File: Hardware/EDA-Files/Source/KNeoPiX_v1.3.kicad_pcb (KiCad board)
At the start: 4 copper layers, 24.5 x 34.6 mm, 35 parts, among them J1 Conn_KNX, J2 Conn_KNX, J3 Screw Terminal - Non Isolated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, J4 Screw Terminal - Isolated IOs, J5 Conn_01x05, J6 Conn_01x05, SW1 Prog BTN, U1 Seeeduino XIAO, U2 LM2937IMP-3.3 / 5.0, U3 ADuM1201AR / ADum1250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

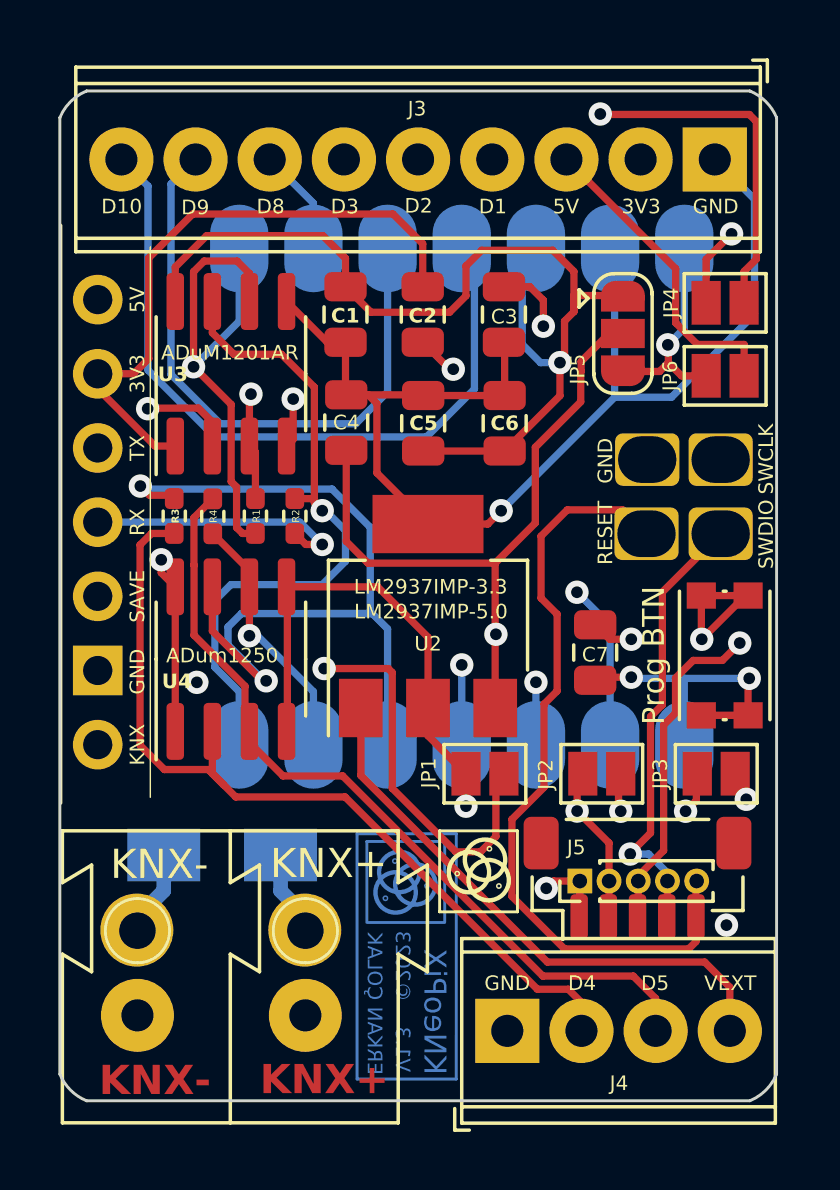
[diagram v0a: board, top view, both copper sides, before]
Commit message: Update - KiCad 8.0x
- Fixed Spelling in sch!
- Ignore Thumbs.db
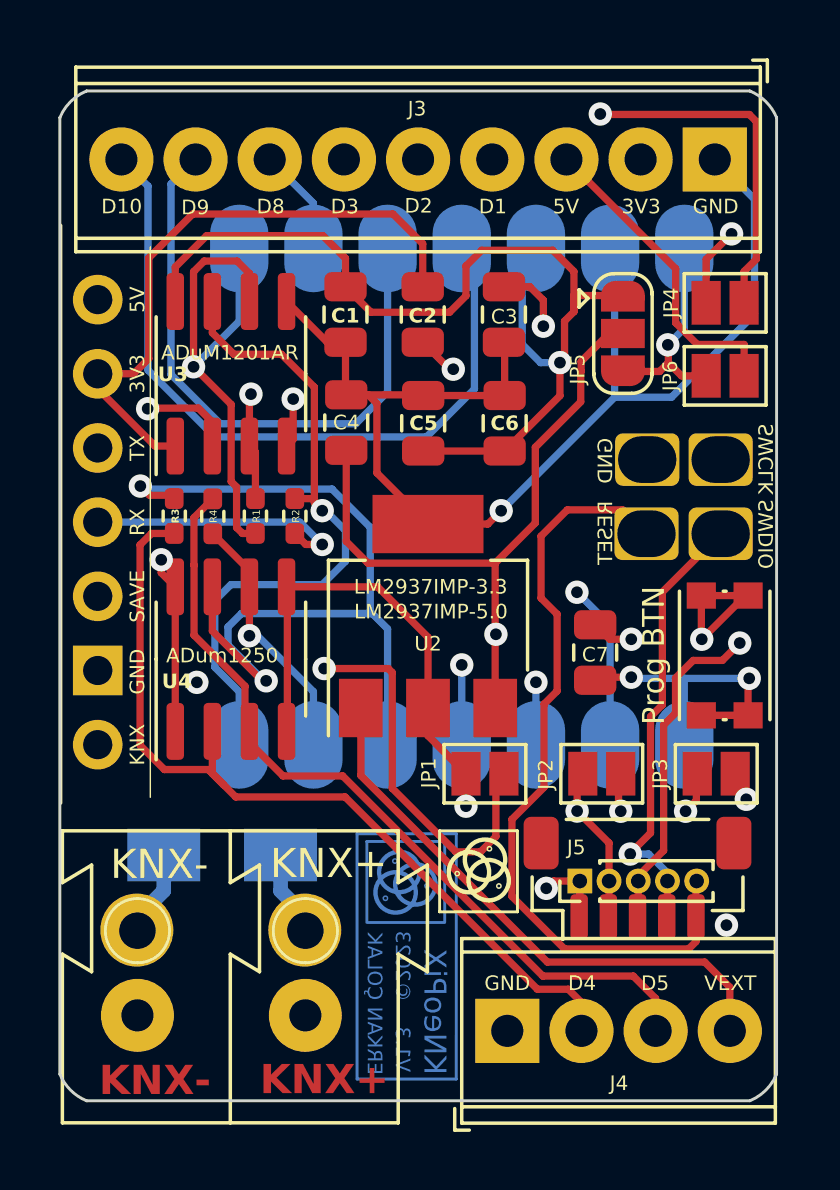
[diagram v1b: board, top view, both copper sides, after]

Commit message: V1.4 - First Prototype Pre Production - In Review
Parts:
- removed the C1 at (58.1, 47.1)
- removed D3: SMAJ40CA-13-F, KNeoPix:D_SMA
- removed J6: Conn_01x05, KNeoPix:PinHeader_1x05_P1.00mm_Vertical
- removed the JP2 at (66.9, 62.8)
- removed JP3: VCC Direct In/Out 3V3/5V, KNeoPix:SolderJumper-2_P1.3mm_Open_Pad1.0x1.5mm
- removed JP6: 5V KNX voltage input, KNeoPix:SolderJumper-2_P1.3mm_Open_Pad1.0x1.5mm
- removed R1: 0Ohm - TXRX Jumper, KNeoPix:R_0402_1005Metric_Pad0.72x0.64mm_HandSolder
- removed R2: 0Ohm - RXTX Jumper, KNeoPix:R_0402_1005Metric_Pad0.72x0.64mm_HandSolder
- removed R3: 0Ohm - D4 Jumper, KNeoPix:R_0402_1005Metric_Pad0.72x0.64mm_HandSolder
- removed R4: 0Ohm - D5 Jumper, KNeoPix:R_0402_1005Metric_Pad0.72x0.64mm_HandSolder
- removed U4: ADum1250, KNeoPix:SOIC-8_3.9x4.9mm_P1.27mm
- added C10: 22uf/16V, Capacitor_SMD:C_0805_2012Metric, F.Cu at (59.7, 47.1)
- added C5: 100nF/16v, Capacitor_SMD:C_01005_0402Metric, F.Cu at (69.0, 57.1)
- added C8: 100nF/50v, Capacitor_SMD:C_0805_2012Metric, F.Cu at (62.0, 63.5)
- added C9: 22uf/16V, Capacitor_SMD:C_0805_2012Metric, F.Cu at (61.9, 47.1)
- added D1: DIODE SCHOTTKY 40V SOD-323HE, lcsc:SOD-323_L1.7-W1.3-LS2.6-RD-1, F.Cu at (70.3, 63.6)
- added D2: DIODE SCHOTTKY 40V SOD-323HE, lcsc:SOD-323_L1.7-W1.3-LS2.6-RD-1, F.Cu at (65.7, 63.6)
- added JP5: SolderJumper_3_Bridged12, Jumper:SolderJumper-3_P1.3mm_Bridged2Bar12_Pad1.0x1.5mm, B.Cu at (64.0, 66.5)
- added L1: CR5040-4R7M, lcsc:IND-SMD_L5.0-W5.0, F.Cu at (66.0, 59.6)
- added U5: AP63205WU-7, lcsc:TSOT-26_L2.9-W1.6-P0.95-LS2.8-BL, F.Cu at (61.2, 52.3)
- C1: renamed from C2; value 100nF -> 100nF/16v; footprint KNeoPix:C_0805_2012Metric -> Capacitor_SMD:C_01005_0402Metric
- C2: renamed from C5; value 100nF -> 100nF/16v; footprint KNeoPix:C_0805_2012Metric -> Capacitor_SMD:C_01005_0402Metric
- C3: value 100 nf 25V -> 100nF/16v; footprint KNeoPix:C_0805_2012Metric -> Capacitor_SMD:C_01005_0402Metric
- C4: value 10µf 16V -> 100nF/16v; footprint KNeoPix:C_0805_2012Metric -> Capacitor_SMD:C_01005_0402Metric
- C6: value 100nF -> 10uf/50V; footprint KNeoPix:C_0805_2012Metric -> Capacitor_SMD:C_0805_2012Metric
- C7: value 100nF 16V - (X5R 0805) -> 10uf/50V; footprint KNeoPix:C_0805_2012Metric -> Capacitor_SMD:C_0805_2012Metric
- J3: value Screw Terminal - Non Isolated IOs -> Screw Terminal - Isolated IOs
- J5: value Conn_01x05 -> ~; footprint KNeoPix:JST_SH_BM05B-SRSS-TB_1x05-1MP_P1.00mm_Vertical -> Connector_JST:JST_SH_BM05B-SRSS-TB_1x05-1MP_P1.00mm_Vertical
- JP1: value GND KNX voltage input -> KNX GND Input; moved to B.Cu
- JP2: renamed from JP5; value Select U2 and Input Voltage -> EXT Input Voltage; moved to B.Cu
- JP4: moved to B.Cu
- SW1: value Prog BTN -> PROG BUTTON; footprint KNeoPix:SW_Push_1P1T_NO_CK_KMR2 -> lcsc:KEY-SMD_4P-L4.2-W3.2-P2.20-LS4.6
- U1: footprint KNeoPix:Seeeduino XIAO-MOUDLE14P-2.54-21X17.8MM-no-15-16-17-18-19-20-pad -> Xiao-ESP32S3-Extendet-Pads:Seeeduino XIAO-MOUDLE14P-2.54-21X17.8MM-no-15-16-17-18-19-20-pad
- U2: value LM2937IMP-3.3 / 5.0 -> TXS0108EPWR; footprint KNeoPix:SOT-223-3_TabPin2 -> lcsc:TSSOP-20_L6.5-W4.4-P0.65-LS6.4-BL
- moved JP4 27.4 mm to (50.6, 64.8)
- moved JP2 18.8 mm to (67.4, 66.5)
- moved C7 11.8 mm to (64.0, 47.1)
- moved JP1 9.11 mm to (70.9, 67.2), turned to -90 degrees
- moved C3 6.84 mm to (57.4, 50.0)
- moved U2 5.52 mm to (55.6, 58.8)
- moved C4 4.49 mm to (57.3, 46.4)
- moved C6 4.40 mm to (66.0, 47.1), turned to 90 degrees
- moved C1 2.60 mm to (59.7, 49.4), turned to 0 degrees
- moved C2 2.39 mm to (58.4, 50.5)
- moved REF2 1.09 mm to (61.6, 53.3)
- moved SW1 0.48 mm to (71.0, 59.2), turned to 90 degrees
- moved J5 0.17 mm to (68.1, 66.5)
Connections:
- net RESET renamed RESET/EN
- net SWCLK renamed CLK/MTDO
- net SWDIO renamed DIO/MTDI
- C2 pad 1: S_3V3 -> 3v3-MCU
- C3 pad 1: EXT_VCC_IN -> EXT_GND
- C3 pad 2: EXT_GND -> 3v3-MCU
- C4 pad 1: EXT_VCC_OUT -> EXT_GND
- C4 pad 2: EXT_GND -> VCC_LS
- C6 pad 1: EXT_GND -> EXT_VCC_IN
- C6 pad 2: S_3V3 -> EXT_GND
- C7 pad 1: D0 -> EXT_VCC_IN
- J3 pad 2: S_3V3 -> 3v3-MCU
- J3 pad 3: KNX_5V -> 5V-MCU
- J3 pad 4: D1 -> DL1
- J3 pad 5: D2 -> DL2
- J3 pad 6: D3 -> DL3
- J3 pad 7: D8 -> DL8
- J3 pad 8: D9 -> DL9
- J3 pad 9: D10 -> DL10
- J4 pad 1: EXT_GND -> EXT_VCC_IN
- J4 pad 2: NEO_DATA0_OUT -> EXT_GND
- J4 pad 3: NEO_DATA1_OUT -> DL4
- J4 pad 4: EXT_VCC_IN -> DL5
- J5 pad 1: EXT_GND -> BOOT/MTMS
- J5 pad 2: S_3V3 -> 3v3/MTCK
- JP2 pad 1: S_3V3 -> Net-(D2-K)
- JP2 pad 2: EXT_VCC_OUT -> 5V-MCU
- JP2 pad 3: 5V-MCU -> Net-(D1-K)
- SW1 pad 1: EXT_GND -> D0
- U1 pad 12: S_3V3 -> 3v3-MCU
- U1 pad 5: D4_SDA -> D4
- U1 pad 6: D5_SCL -> D5
- U2 pad 1: EXT_VCC_IN -> D1
- U2 pad 2: EXT_GND -> 3v3-MCU
- U2 pad 3: EXT_VCC_OUT -> D2
- U3 pad 8: S_3V3 -> 3v3-MCU
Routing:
- net S_3V3: track 94.2 -> 0.00 mm, vias 3 -> 0
- net 3v3-MCU: track 0.00 -> 61.2 mm, vias 0 -> 4
- net VCC_LS: track 0.00 -> 42.9 mm, vias 0 -> 3
- net EXT_VCC_IN: track 67.4 -> 28.9 mm, vias 2 -> 1
- net KNX_3V3: track 52.8 -> 15.3 mm, vias 2 -> 1
- net DL2: track 0.00 -> 36.6 mm, vias 0 -> 1
- net EXT_VCC_OUT: track 36.4 -> 0.00 mm, vias 2 -> 0
- net DL5: track 0.00 -> 35.0 mm, vias 0 -> 1
- net DL1: track 0.00 -> 34.7 mm, vias 0 -> 1
- net EXT_GND: track 110.9 -> 78.3 mm, vias 6 -> 1
- net DL3: track 0.00 -> 32.1 mm, vias 0 -> 1
- net 5V-MCU: track 7.31 -> 38.5 mm, vias 1 -> 2
- net D4_SDA: track 31.0 -> 0.00 mm, vias 2 -> 0
- net NEO_DATA0_OUT: track 29.9 -> 0.00 mm
- net NEO_DATA1_OUT: track 27.5 -> 0.00 mm
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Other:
- board text added: "XIAO RP2040 XIAO RP2350 XIAO ESP32S3 XIAO ESP32S3 Plus"
- board text removed: "XIAO RP2040 XIAO SAMD21"

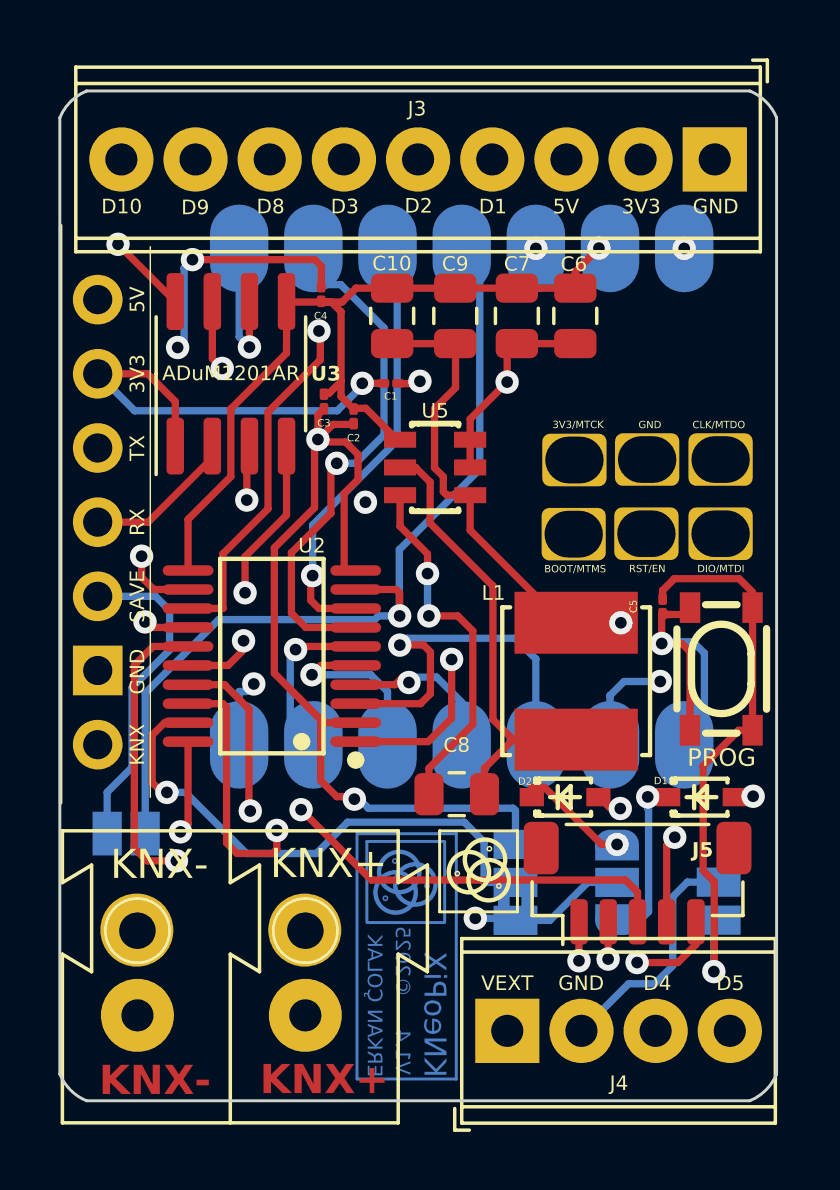
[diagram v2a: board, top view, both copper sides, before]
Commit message: Fixed - Prog button GND bug (after Review)
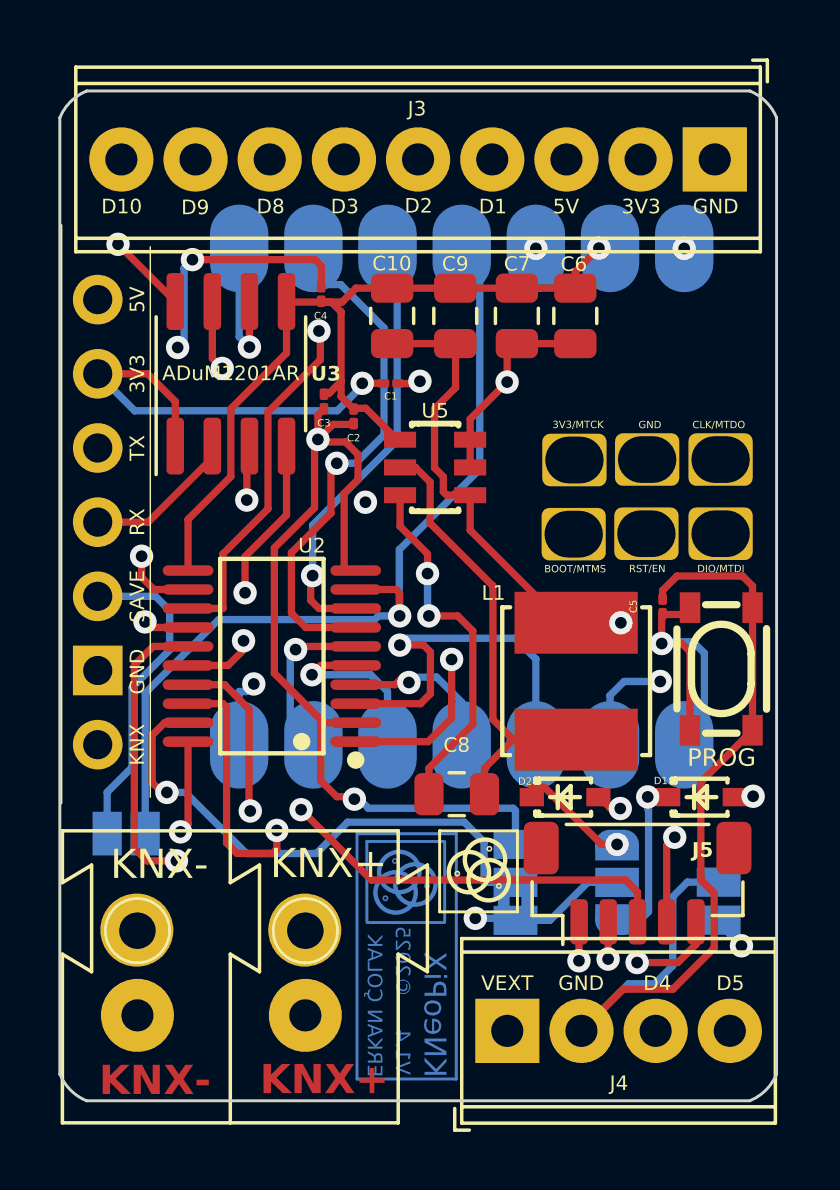
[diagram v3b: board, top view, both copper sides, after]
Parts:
- U3: value ADuM1201AR / ADum1250 -> ADUM1250ARZ-RL7 - (ADuM1201AR / ADum1250AR) AR suffix required
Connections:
- C5 pad 2: KNX_GND -> EXT_GND
- SW1 pad 3: KNX_GND -> EXT_GND
- SW1 pad 4: KNX_GND -> EXT_GND
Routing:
- net EXT_GND: track 78.3 -> 101.0 mm
- net KNX_GND: track 75.8 -> 58.3 mm
- net D0: track 11.2 -> 9.91 mm
- net DIO/MTDI: track 14.2 -> 13.4 mm

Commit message: AP63205WU-7 (U5) repositioned for better thermal management
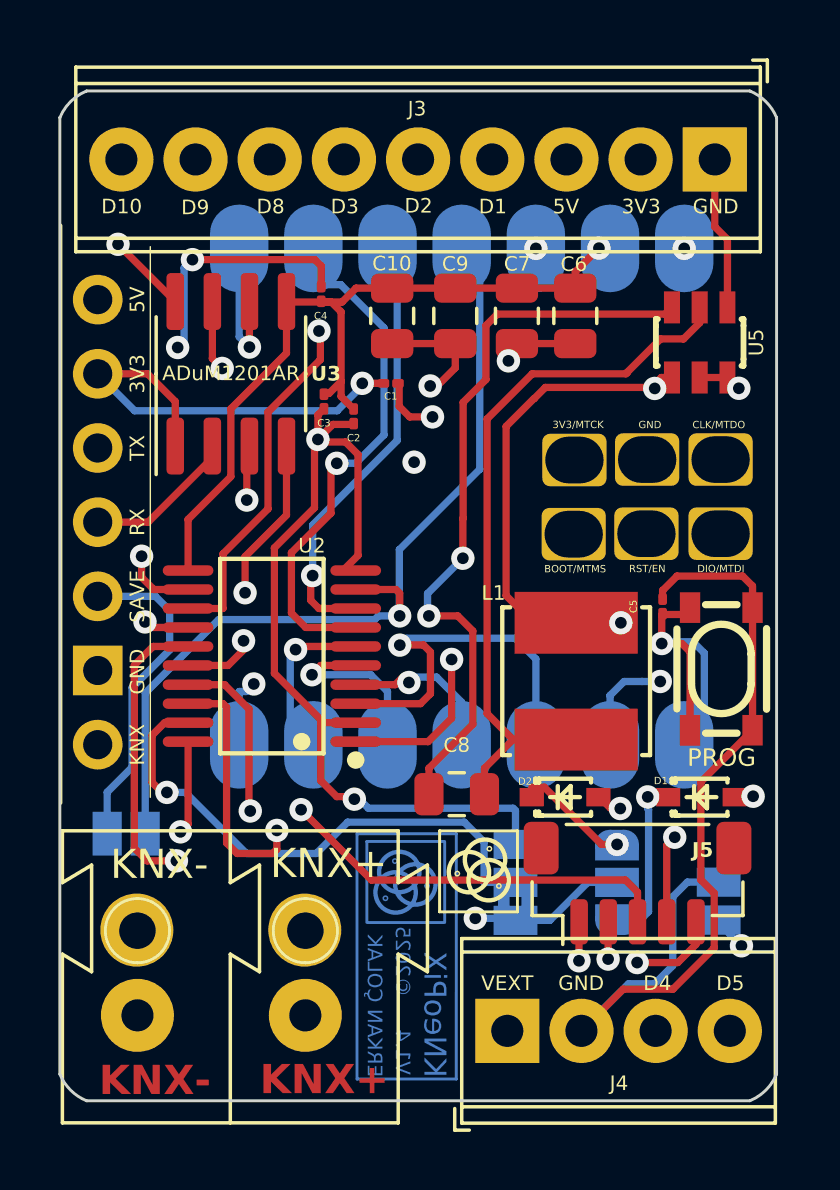
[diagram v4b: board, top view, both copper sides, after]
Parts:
- moved U5 10.0 mm to (70.3, 48.0), turned to 0 degrees
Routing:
- net Net-(U5-BST): track 12.5 -> 25.3 mm
- net EXT_5V: track 21.9 -> 33.0 mm, vias 2 -> 4
- net Net-(U5-SW): track 15.7 -> 25.0 mm
- net EXT_VCC_IN: track 28.9 -> 35.1 mm, vias 1 -> 2
- net EXT_GND: track 101.0 -> 106.9 mm
- net CLK/MTDO: track 43.1 -> 40.7 mm
- net RESET/EN: track 20.2 -> 21.0 mm

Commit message: Cleaned up tracks.
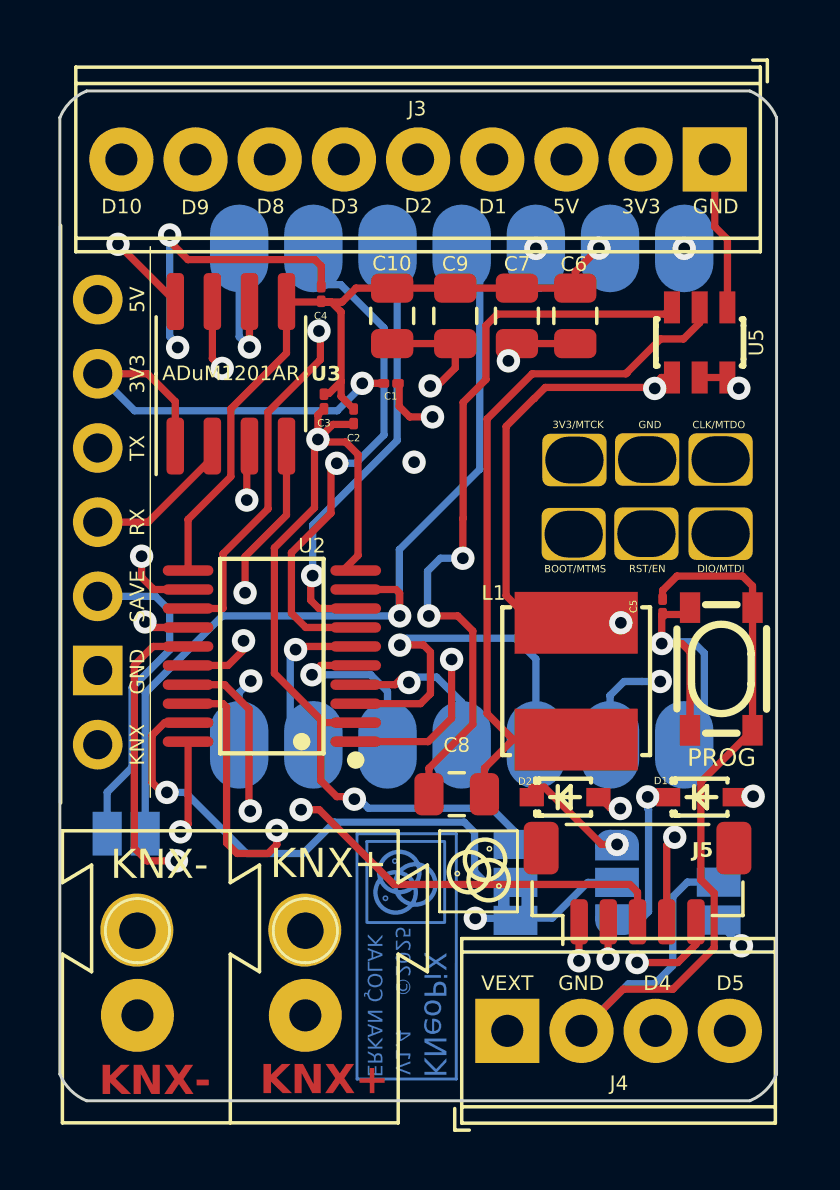
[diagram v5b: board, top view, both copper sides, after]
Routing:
- net VCC_LS: track 42.9 -> 44.9 mm
- net DL8: track 20.7 -> 19.5 mm
- net DL2: track 36.6 -> 35.4 mm
- net DL9: track 21.4 -> 20.5 mm
